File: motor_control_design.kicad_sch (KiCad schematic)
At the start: 87 parts, among them J1 TYPE-C-31-M-12, J10 3V3, J2 SWD, J3 VBAT, J4 GND, J5 FC_M/P, J6 Conn_01x06, J8 Conn_01x06, J9 GND, Q1 RF1S9540SM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

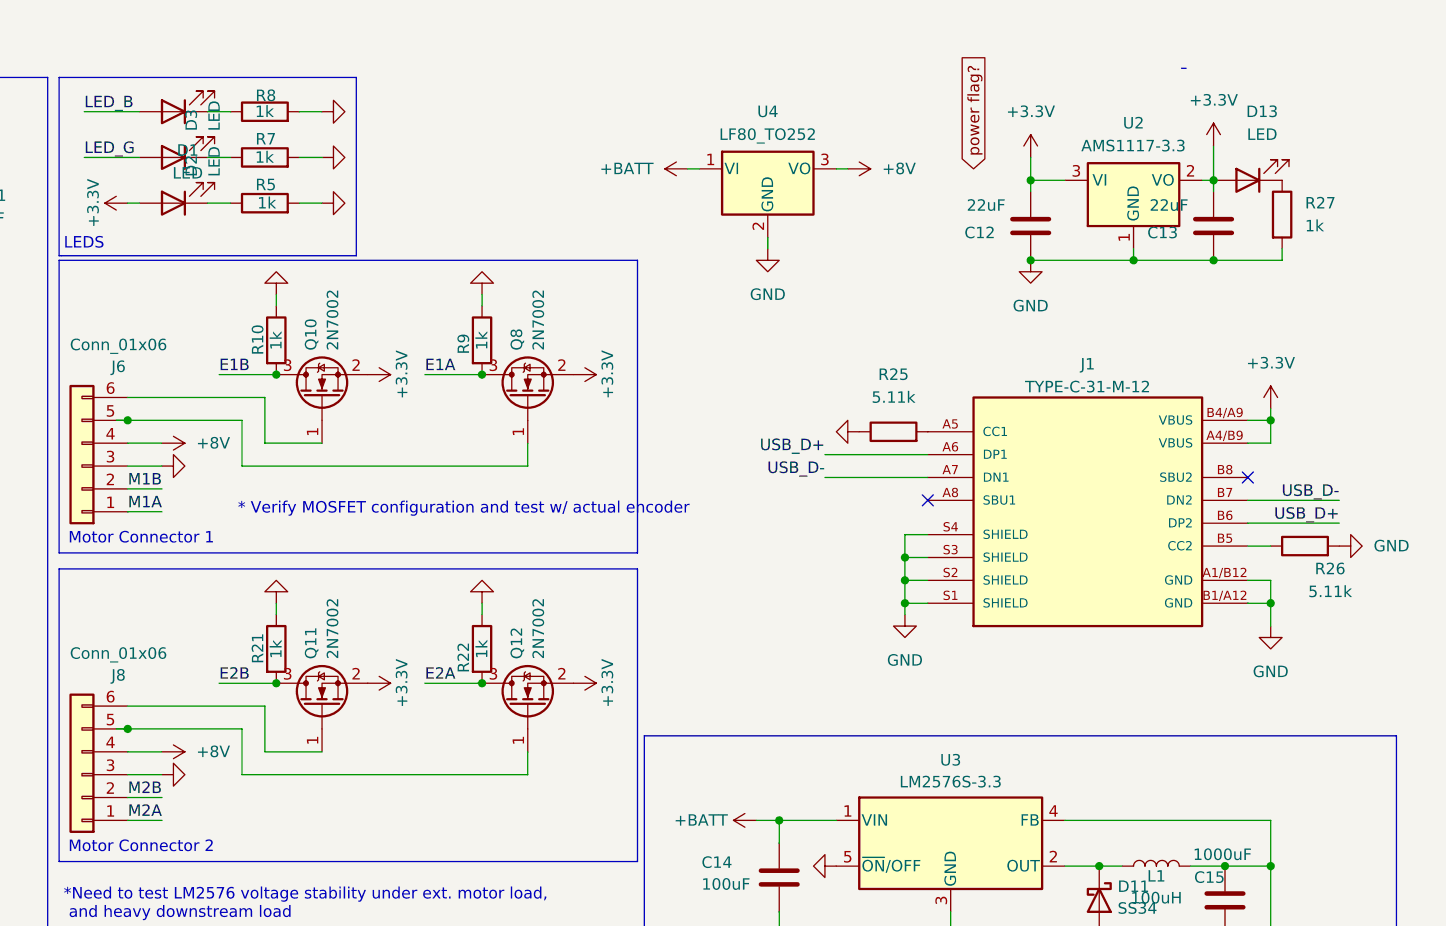
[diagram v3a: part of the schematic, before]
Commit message: Working on new 5v 3.3v power sys
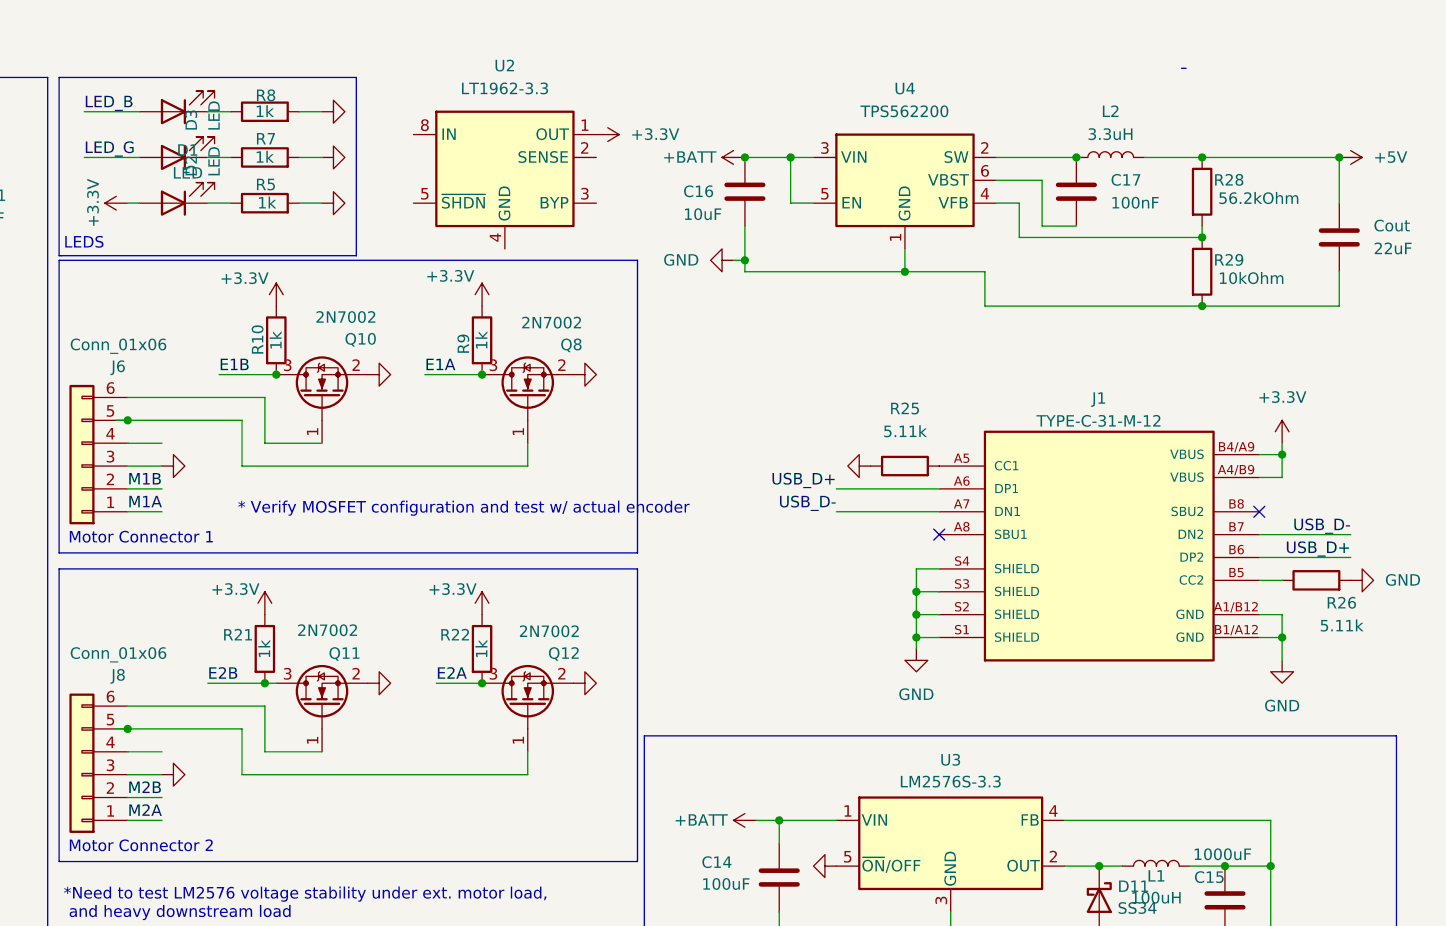
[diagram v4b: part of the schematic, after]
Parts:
- removed C12, C13: 22uF, symbol Device:C
- removed D13: LED, symbol Device:LED
- removed R27: 1k, symbol Device:R
- removed U2: AMS1117-3.3, Package_TO_SOT_SMD:SOT-223-3_TabPin2, symbol Regulator_Linear:AMS1117-3.3
- removed U4: LF80_TO252, Package_TO_SOT_SMD:TO-252-2, symbol Regulator_Linear:LF80_TO252
- added C16: 10uF, symbol Device:C
- added C17: 100nF, symbol Device:C
- added Cout: 22uF, symbol Device:C
- added L2: 3.3uH, symbol Device:L
- added R28: 56.2kOhm, symbol Device:R
- added R29: 10kOhm, symbol Device:R
- added U2: LT1962-3.3, Package_SO:MSOP-8_3x3mm_P0.65mm, symbol Regulator_Linear:LT1962-3.3
- added U4: TPS562200, Package_TO_SOT_SMD:SOT-23-6, symbol Regulator_Switching:TPS562200
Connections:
- net +3.3V: now also R10.1, R21.1, R22.1, R9.1, U2.1 (OUT); no longer Q10.2 (S), Q11.2 (S), Q12.2 (S), Q8.2 (S)
- net +BATT: now also C16.1, U4.3 (VIN), U4.5 (EN)
- net GND: now also Q10.2 (S), Q11.2 (S), Q12.2 (S), Q8.2 (S), C16.2, Cout.2, R29.2, U4.1 (GND); no longer R10.1, R21.1, R22.1, R9.1
- net +8V: no longer names the net of J8.4 (Pin_4)
- net +8V: no longer J6.4 (Pin_4)
- new net: C17.1, L2.1, U4.2 (SW)
- new net: R28.2, R29.1, U4.4 (VFB)
- new net: C17.2, U4.6 (VBST)
- new net +5V: Cout.1, L2.2, R28.1
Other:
- moved on the sheet: J1, R21, R25, R26

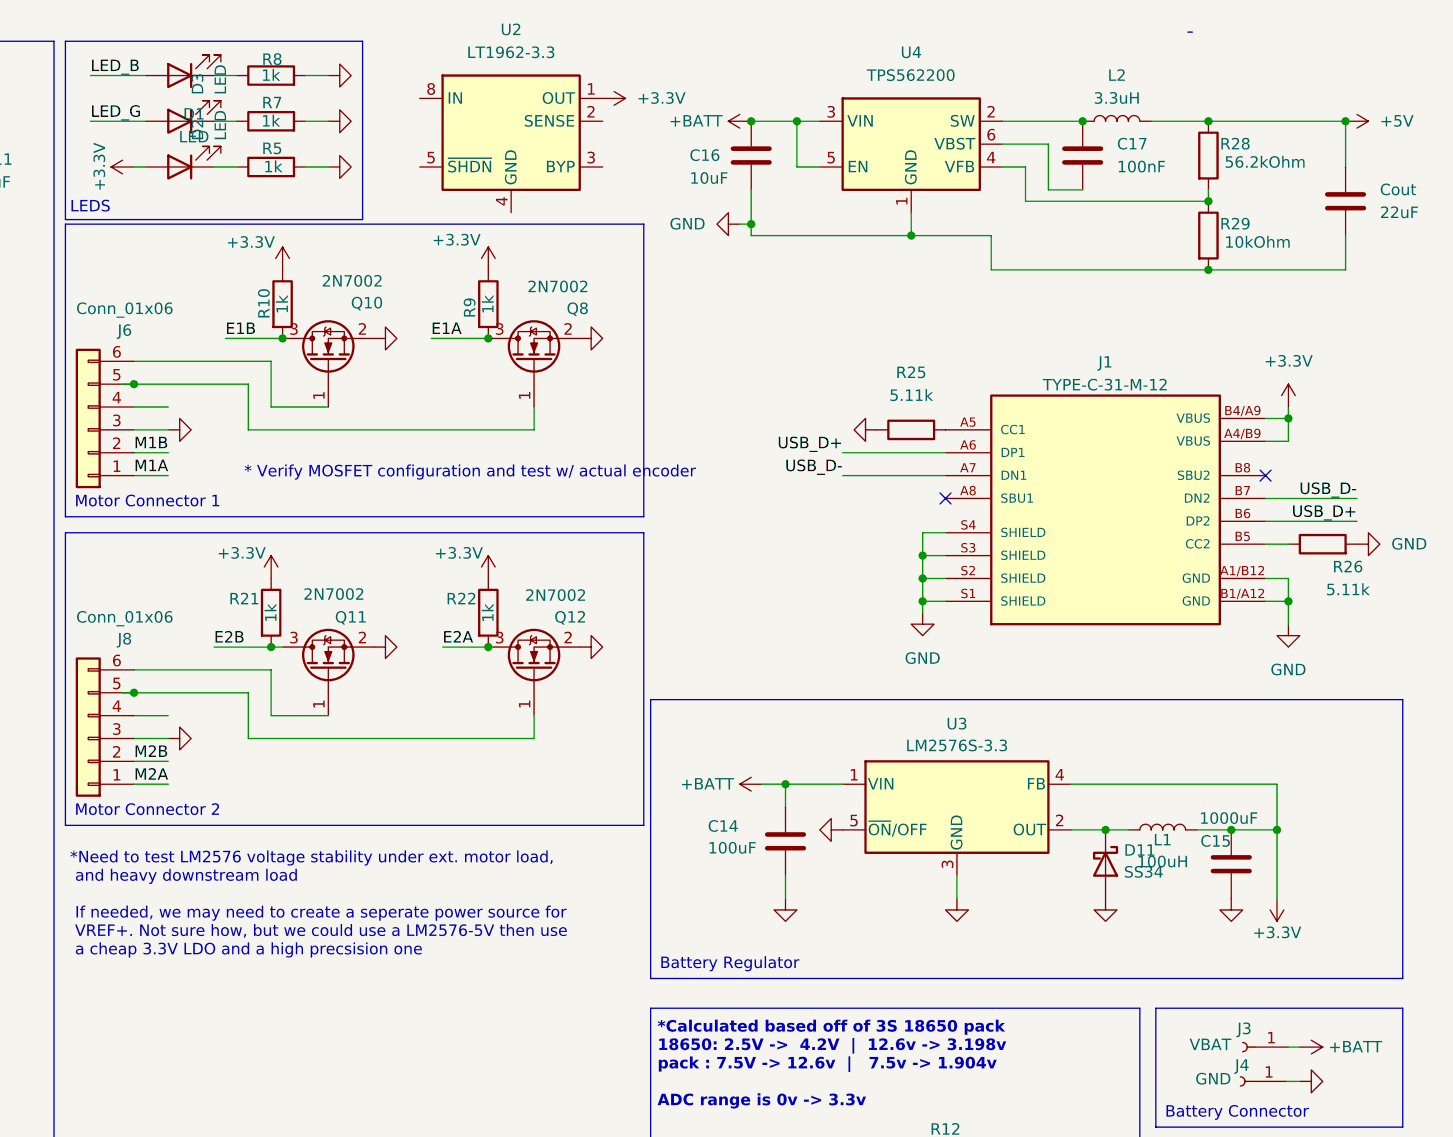
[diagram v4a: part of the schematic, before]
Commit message: Systems boxed, footprints added
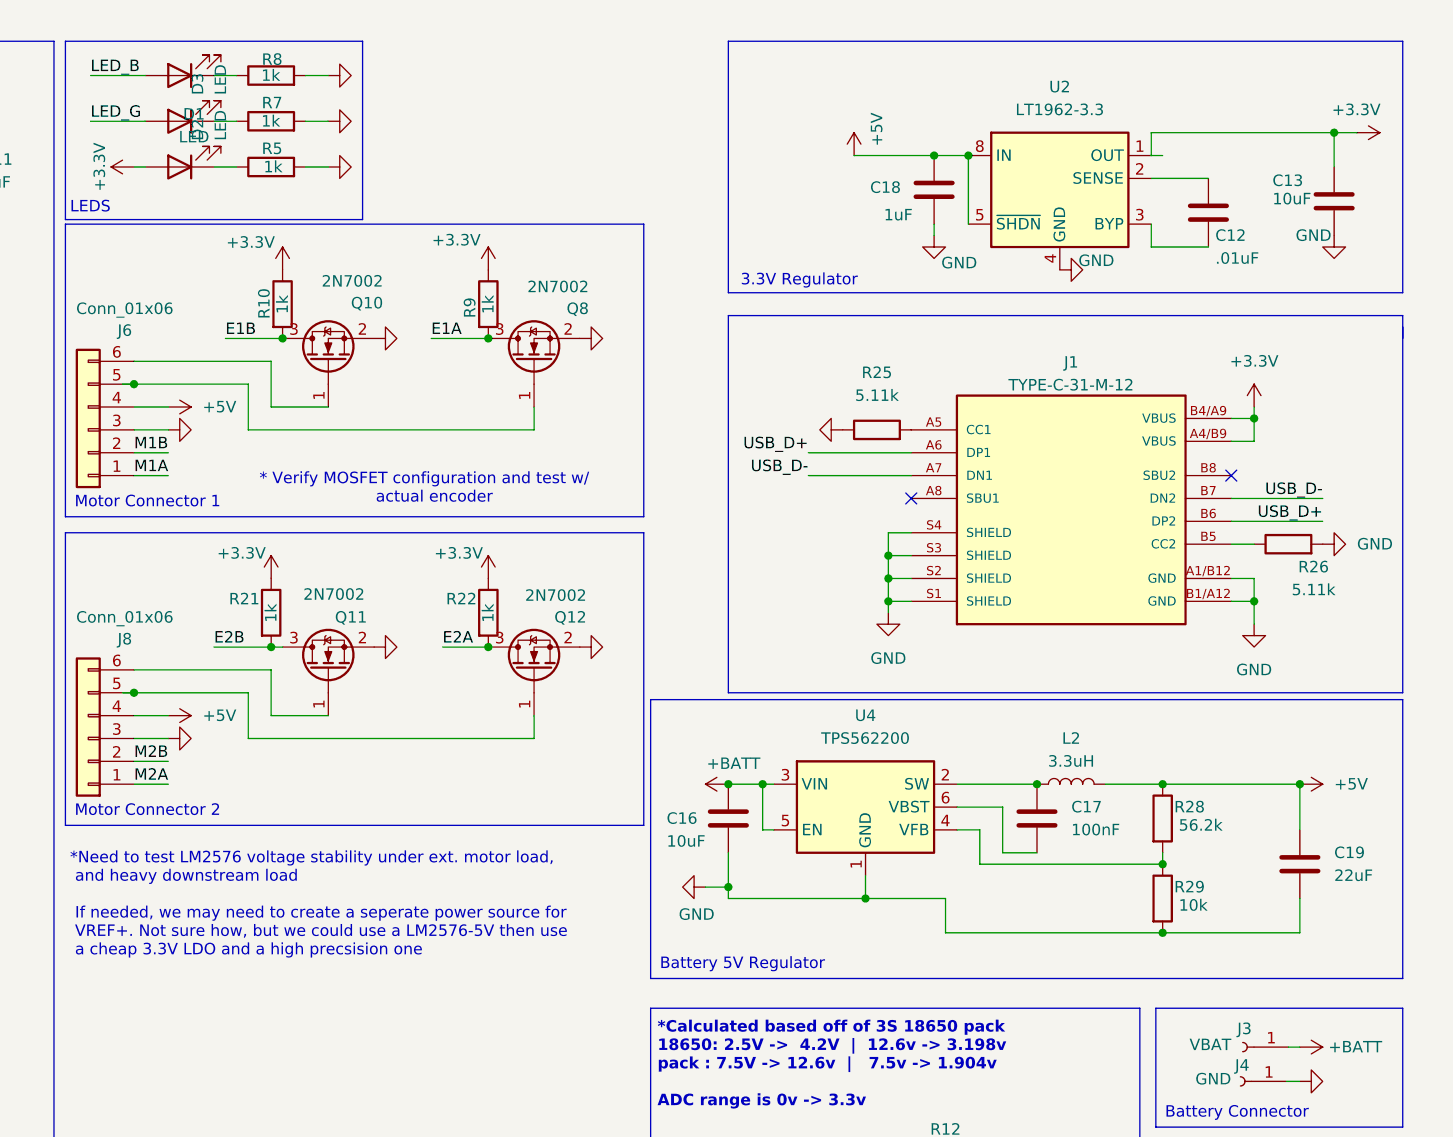
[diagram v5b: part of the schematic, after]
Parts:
- removed C14: 100uF, Capacitor_SMD:C_0805_2012Metric, symbol Device:C
- removed C15: 1000uF, Capacitor_SMD:CP_Elec_10x10.5, symbol Device:C
- removed D11: SS34, Diode_SMD:D_SMA, symbol Diode:SS34
- removed L1: 100uH, Inductor_SMD:L_TaiTech_TMPC1265_13.5x12.5mm, symbol Device:L
- removed U3: LM2576S-3.3, Package_TO_SOT_SMD:TO-263-5_TabPin3, symbol Regulator_Switching:LM2576S-3.3
- added C12: .01uF, Capacitor_SMD:C_0402_1005Metric, symbol Device:C
- added C13: 10uF, Capacitor_SMD:C_0402_1005Metric, symbol Device:C
- added C18: 1uF, Capacitor_SMD:C_0402_1005Metric, symbol Device:C
- C16, C17: footprint (none) -> Capacitor_SMD:C_0402_1005Metric
- C19: renamed from Cout; footprint (none) -> Capacitor_SMD:C_0402_1005Metric
- L2: footprint (none) -> Inductor_SMD:L_0402_1005Metric
- R25, R26: footprint (none) -> Resistor_SMD:R_0402_1005Metric
- R28: value 56.2kOhm -> 56.2k; footprint (none) -> Resistor_SMD:R_0402_1005Metric
- R29: value 10kOhm -> 10k; footprint (none) -> Resistor_SMD:R_0402_1005Metric
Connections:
- net +3.3V: now also C13.1
- net +5V: now also J6.4 (Pin_4), J8.4 (Pin_4), U2.5 (~{SHDN}), U2.8 (IN), C18.1
- net GND: now also U2.4 (GND), C13.2, C18.2
- net at U2.2 (SENSE): now also C12.1
- net at U2.3 (BYP): now also C12.2
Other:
- note added: "3.3V Regulator"
- note added: "Battery 5V Regulator"
- note removed: "Battery Regulator"
- moved on the sheet: C16, C17, C19, J1, L2, R25, R26, R28, R29, U2, U4

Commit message: Routing, still messy
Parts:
- J1: footprint USBC:HRO_TYPE-C-31-M-12 -> Connector_USB:USB_C_Receptacle_HRO_TYPE-C-31-M-12
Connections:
- net VBatt_sense: no longer U1.14 (PA4)
- no-connect marks 13 -> 14
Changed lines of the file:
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@@
 	)
 	(no_connect
+		(at 100.33 87.63)
+	)
+	(no_connect
 		(at 67.31 82.55)
 	)
@@
 	(wire
 		(pts
-			(xy 113.03 87.63) (xy 100.33 87.63)
-		)
-		(stroke
-			(width 0)
-			(type default)
-		)
-	)
-	(wire
-		(pts
 			(xy 60.96 92.71) (xy 67.31 92.71)
 		)
@@
 		)
 	)
-	(label "VBatt_sense"
-		(at 113.03 87.63 180)
-		(fields_autoplaced yes)
-		(effects
-			(font
-				(size 1.27 1.27)
-			)
-			(justify right bottom)
-		)
-	)
 	(label "NRST"
 		(at 234.95 162.56 0)
@@
 			)
 		)
-		(property "Footprint" "USBC:HRO_TYPE-C-31-M-12"
+		(property "Footprint" "Connector_USB:USB_C_Receptacle_HRO_TYPE-C-31-M-12"
 			(at 224.79 43.18 0)
 			(effects

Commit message: fixed LEDS?
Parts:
- D1: LCSC Part C2286 -> C9900011154
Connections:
- net +3.3V: no longer J1.A4/B9 (VBUS), J1.B4/A9 (VBUS)
- net +5V: now also J1.A4/B9 (VBUS), J1.B4/A9 (VBUS)
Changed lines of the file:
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@@
 		(on_board yes)
 		(dnp no)
-		(fields_autoplaced yes)
 		(property "Reference" "D1"
-			(at 147.6375 22.0812 0)
+			(at 143.256 28.956 0)
 			(effects
 				(font
@@
 		)
 		(property "Value" "LED"
-			(at 147.6375 24.6181 0)
+			(at 146.05 25.908 0)
 			(effects
 				(font
@@
 			)
 		)
-		(property "LCSC Part" "C2286"
+		(property "LCSC Part" "C9900011154"
+			(at 146.05 27.94 0)
+			(effects
+				(font
+					(size 1.27 1.27)
+				)
+				(hide yes)
+			)
+		)
+		(property "Field6" ""
 			(at 146.05 27.94 0)
 			(effects
@@
 		(dnp no)
 		(property "Reference" "D3"
-			(at 148.0728 19.939 90)
+			(at 141.986 18.796 0)
 			(effects
 				(font
@@
 		)
 		(property "Value" "LED"
-			(at 150.6097 19.939 90)
+			(at 144.018 14.986 0)
 			(effects
 				(font
@@
 	)
 	(symbol
-		(lib_name "+3.3V_2")
-		(lib_id "power:+3.3V")
-		(at 265.43 54.61 0)
-		(unit 1)
-		(exclude_from_sim no)
-		(in_bom yes)
-		(on_board yes)
-		(dnp no)
-		(fields_autoplaced yes)
-		(property "Reference" "#PWR067"
-			(at 265.43 58.42 0)
-			(effects
-				(font
-					(size 1.27 1.27)
-				)
-				(hide yes)
-			)
-		)
-		(property "Value" "+3.3V"
-			(at 265.43 49.53 0)
-			(effects
-				(font
-					(size 1.27 1.27)
-				)
-			)
-		)
-		(property "Footprint" ""
-			(at 265.43 54.61 0)
-			(effects
-				(font
-					(size 1.27 1.27)
-				)
-				(hide yes)
-			)
-		)
-		(property "Datasheet" ""
-			(at 265.43 54.61 0)
-			(effects
-				(font
-					(size 1.27 1.27)
-				)
-				(hide yes)
-			)
-		)
-		(property "Description" "Power symbol creates a global label with name \"+3.3V\""
-			(at 265.43 54.61 0)
-			(effects
-				(font
-					(size 1.27 1.27)
-				)
-				(hide yes)
-			)
-		)
-		(pin "1"
-		)
-		(instances
-			(project ""
-				(path "/e96577c4-ec21-4b26-996c-9ebc38d9c737"
-					(reference "#PWR067")
-					(unit 1)
-				)
-			)
-		)
-	)
-	(symbol
 		(lib_id "Transistor_FET:2N7002")
 		(at 162.56 151.13 90)
@@
 		(dnp no)
 		(property "Reference" "D2"
-			(at 148.0728 25.019 90)
+			(at 141.732 24.13 0)
 			(effects
 				(font
@@
 		)
 		(property "Value" "LED"
-			(at 150.6097 25.019 90)
+			(at 143.002 20.574 0)
 			(effects
 				(font
@@
 					(unit 1)
 				)
+			)
+		)
+	)
+	(symbol
+		(lib_id "power:+5V")
+		(at 265.43 54.61 0)
+		(unit 1)
+		(exclude_from_sim no)
+		(in_bom yes)
+		(on_board yes)
+		(dnp no)
+		(property "Reference" "#PWR029"
+			(at 265.43 58.42 0)
+			(effects
+				(font
+					(size 1.27 1.27)
+				)
+				(hide yes)
+			)
+		)
+		(property "Value" "+5V"
+			(at 267.97 53.594 90)
+			(effects
+				(font
+					(size 1.27 1.27)
+				)
+				(justify left)
+			)
+		)
+		(property "Footprint" ""
+			(at 265.43 54.61 0)
+			(effects
+				(font
+					(size 1.27 1.27)
+				)
+				(hide yes)
+			)
+		)
+		(property "Datasheet" ""
+			(at 265.43 54.61 0)
+			(effects
+				(font
+					(size 1.27 1.27)
+				)
+				(hide yes)
+			)
+		)
+		(property "Description" "Power symbol creates a global label with name \"+5V\""
+			(at 265.43 54.61 0)
+			(effects
+				(font
+					(size 1.27 1.27)
+				)
+				(hide yes)
+			)
+		)
+		(pin "1"
+		)
+		(instances
+			(project "motor_control_design"
+				(path "/e96577c4-ec21-4b26-996c-9ebc38d9c737"
+					(reference "#PWR029")
+					(unit 1)
+				)
